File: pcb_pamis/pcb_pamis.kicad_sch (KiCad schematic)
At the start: 1 part, among them U1 ESP32-WROOM-32UE

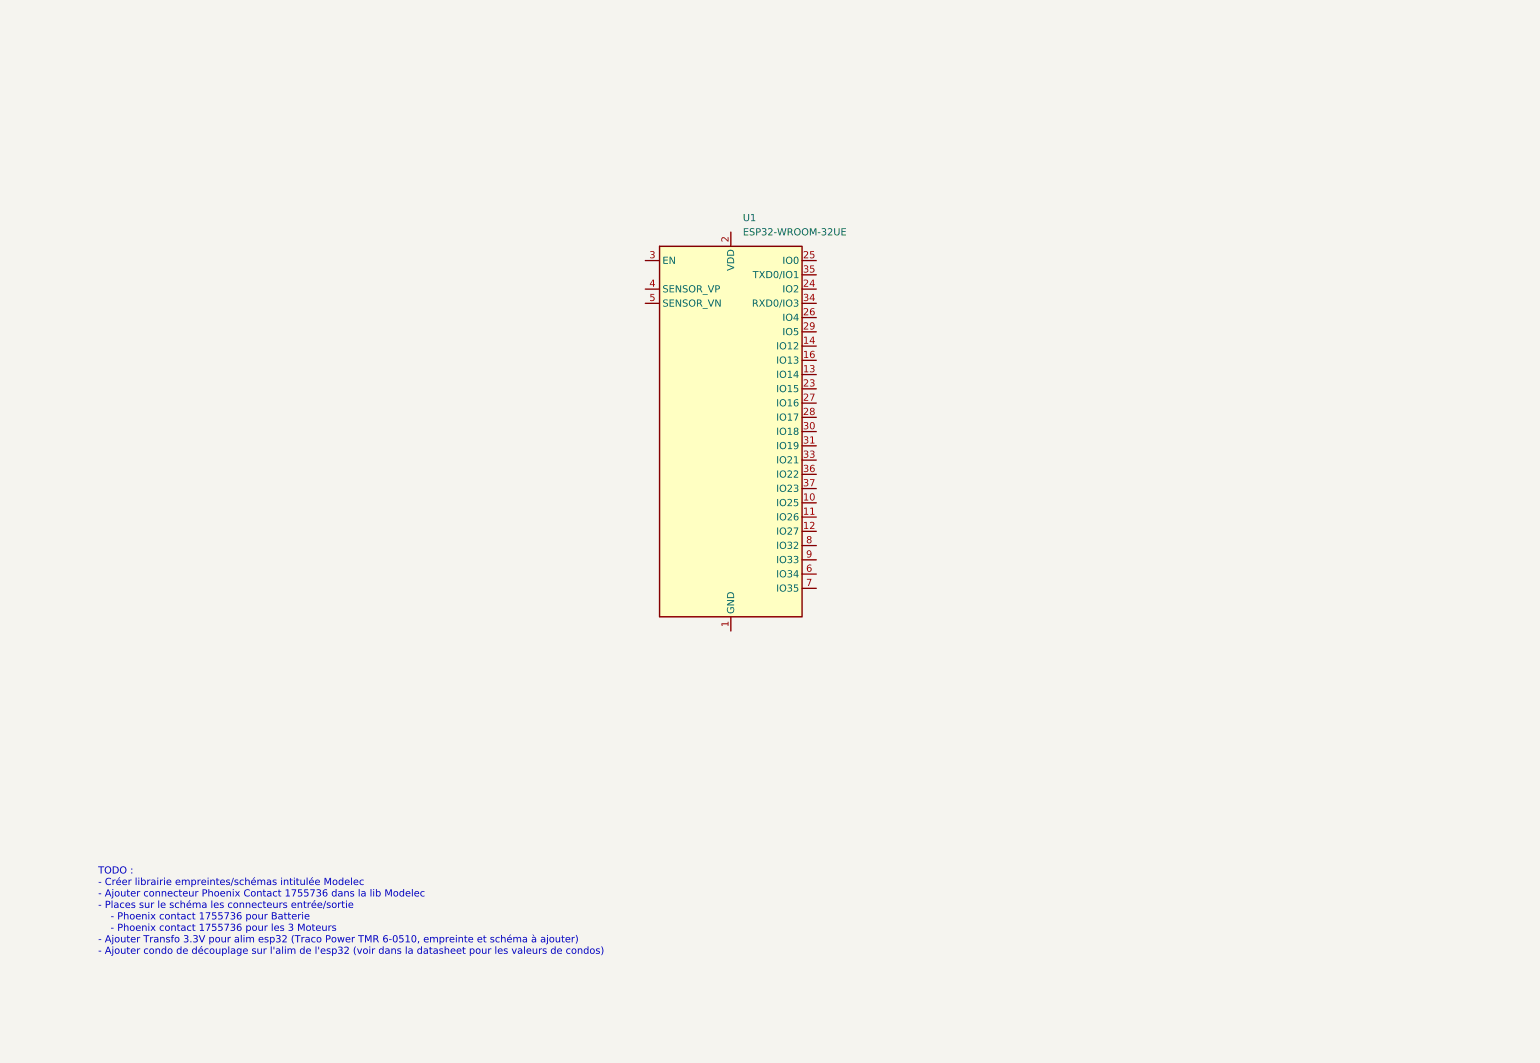
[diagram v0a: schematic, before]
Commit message: work on power supply
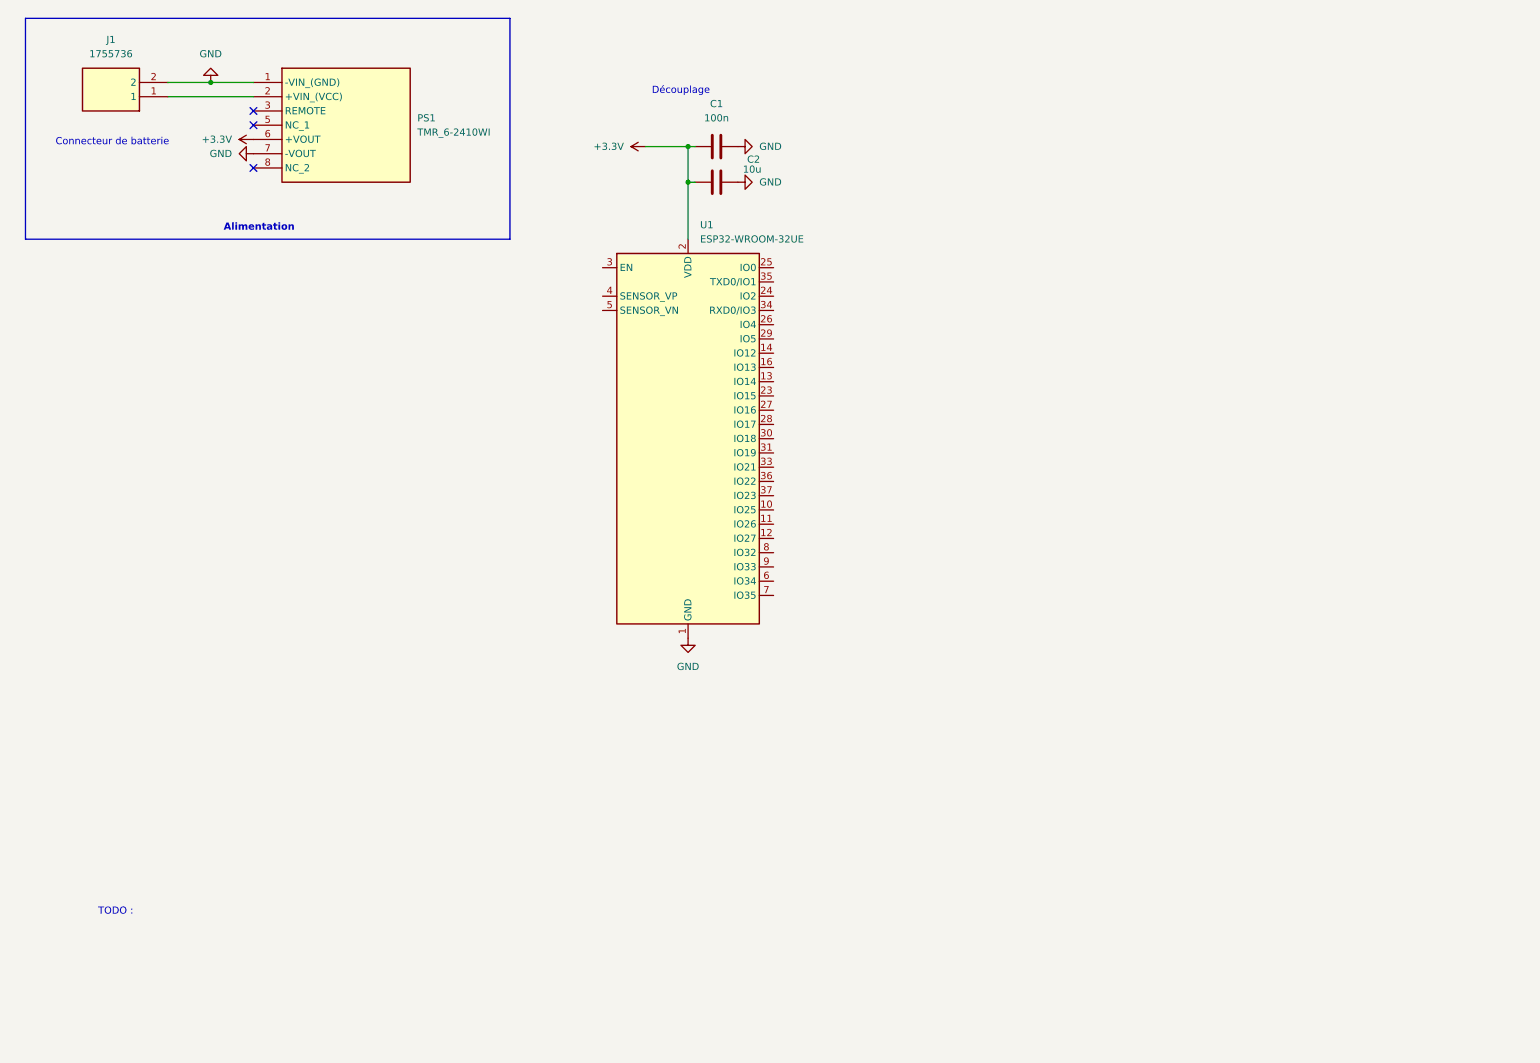
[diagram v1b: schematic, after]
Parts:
- added C1: 100n, Capacitor_SMD:C_0805_2012Metric_Pad1.18x1.45mm_HandSolder, symbol Device:C
- added C2: 10u, Capacitor_SMD:C_0805_2012Metric_Pad1.18x1.45mm_HandSolder, symbol Device:C
- added J1: 1755736, Modelec:PhoenixContact_MSTBVA_2,5_2-G-5,08_1x02_P5.08mm_Vertical, symbol Modelec:1755736
- added PS1: TMR_6-2410WI, TMR60510, symbol Modelec:TMR_6-0510
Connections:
- net GND: now reaches U1.1 (GND), U1.15 (GND), U1.38 (GND), U1.39 (GND)
- net GND: now also C1.2, C2.2, J1.2, PS1.1 (-VIN_(GND)), PS1.7 (-VOUT)
- net +3.3V: now reaches U1.2 (VDD)
- net +3.3V: now also C1.1, C2.1, PS1.6 (+VOUT)
- new net: J1.1, PS1.2 (+VIN_(VCC))
- no-connect marks 0 -> 3
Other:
- note added: "Alimentation"
- note added: "Connecteur de batterie"
- note added: "Découplage"
- note added: "TODO :"
- note removed: "TODO : - Créer librairie empreintes/schémas intitulée Modelec - Ajouter connecteur Phoenix Contact 1755736 dans la lib Modelec - Places sur le schéma les connecteurs entrée/sortie - Phoenix contact 1755736 pour Batterie - Phoenix contact 1755736 pour les 3 Moteurs - Ajouter Transfo 3.3V pour alim esp32 (Traco Power TMR 6-0510, empreinte et schéma à ajouter) - Ajouter condo de découplage sur l'ali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"
- moved on the sheet: U1

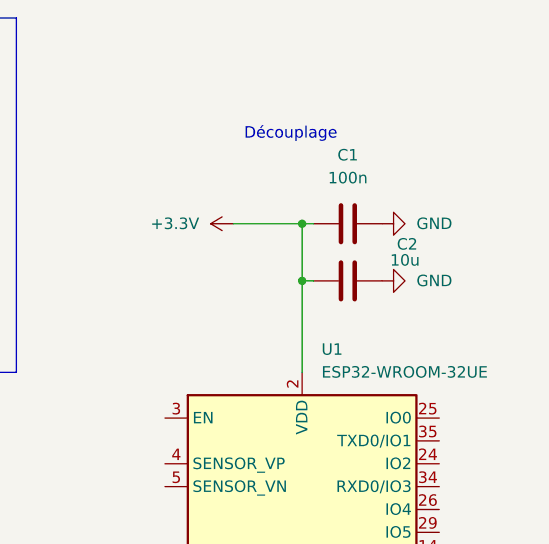
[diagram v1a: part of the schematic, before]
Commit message: fix: decouplage esp32
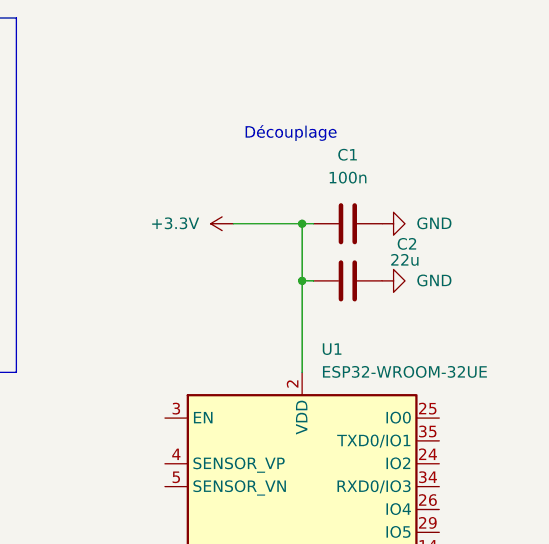
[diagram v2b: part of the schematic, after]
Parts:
- C2: value 10u -> 22u
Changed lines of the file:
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@@
 			)
 		)
-		(property "Value" "10u"
+		(property "Value" "22u"
 			(at 144.78 40.894 90)
 			(effects

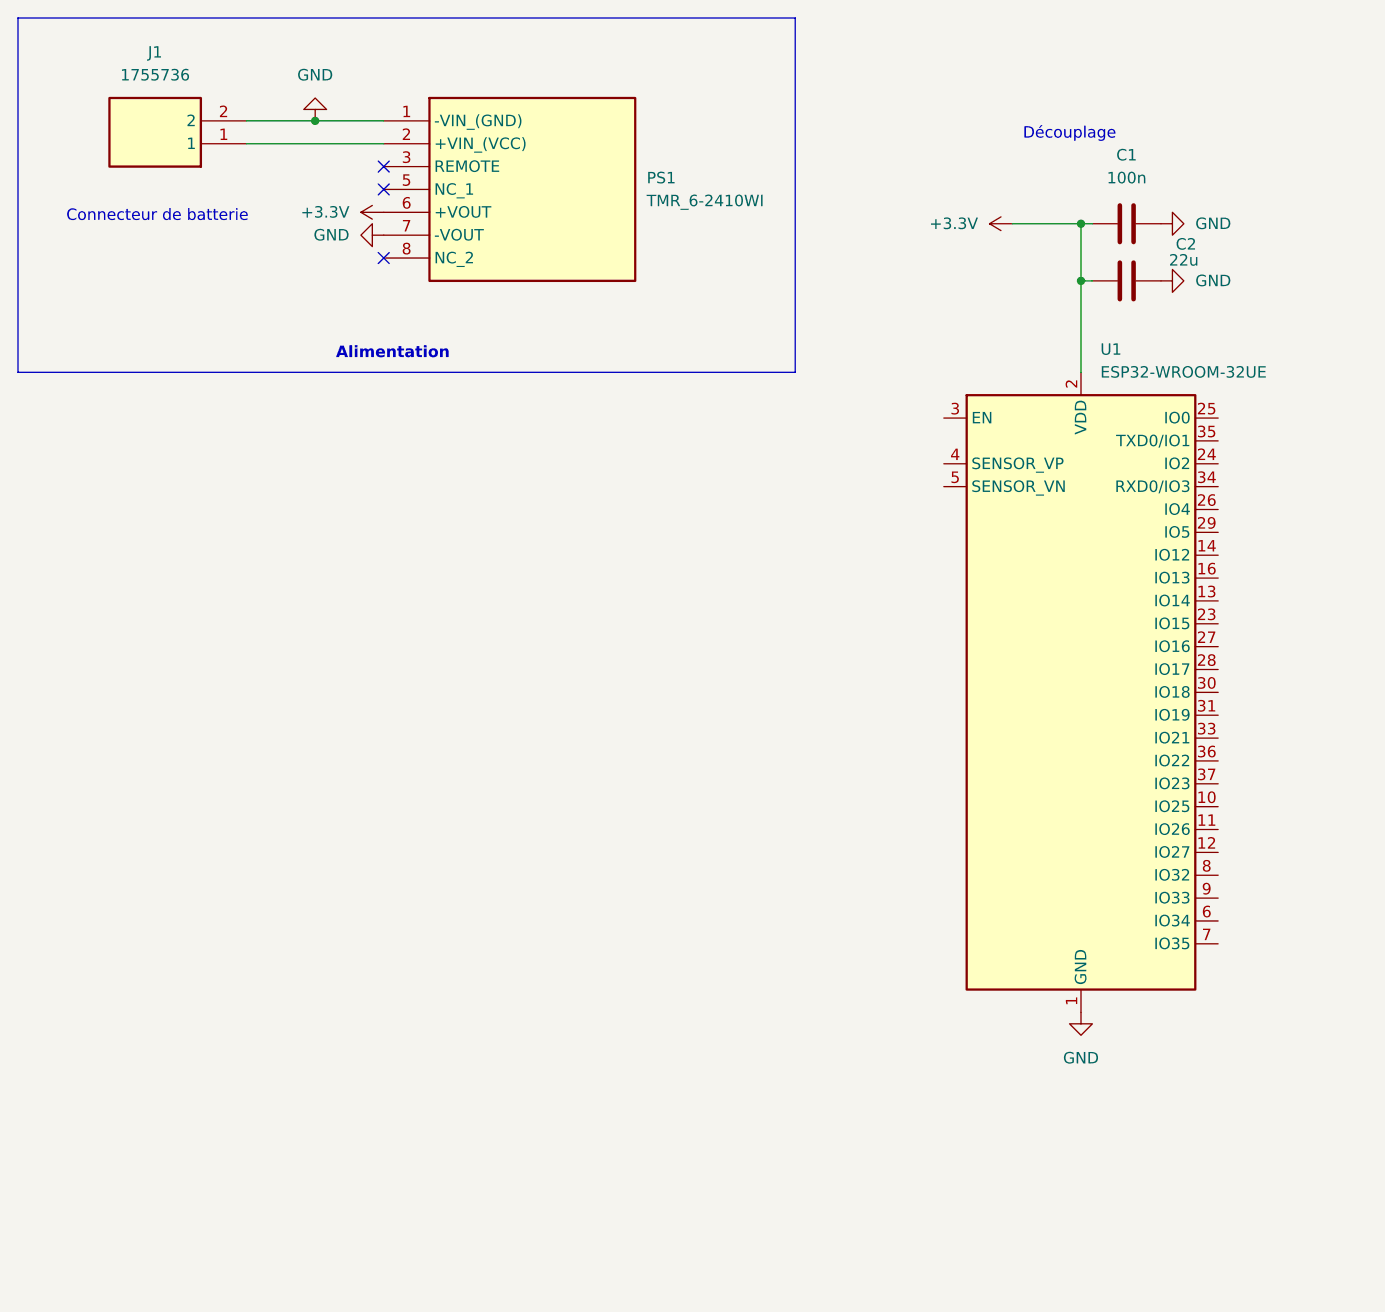
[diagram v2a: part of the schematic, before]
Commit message: feat: add usb port + add RESET button
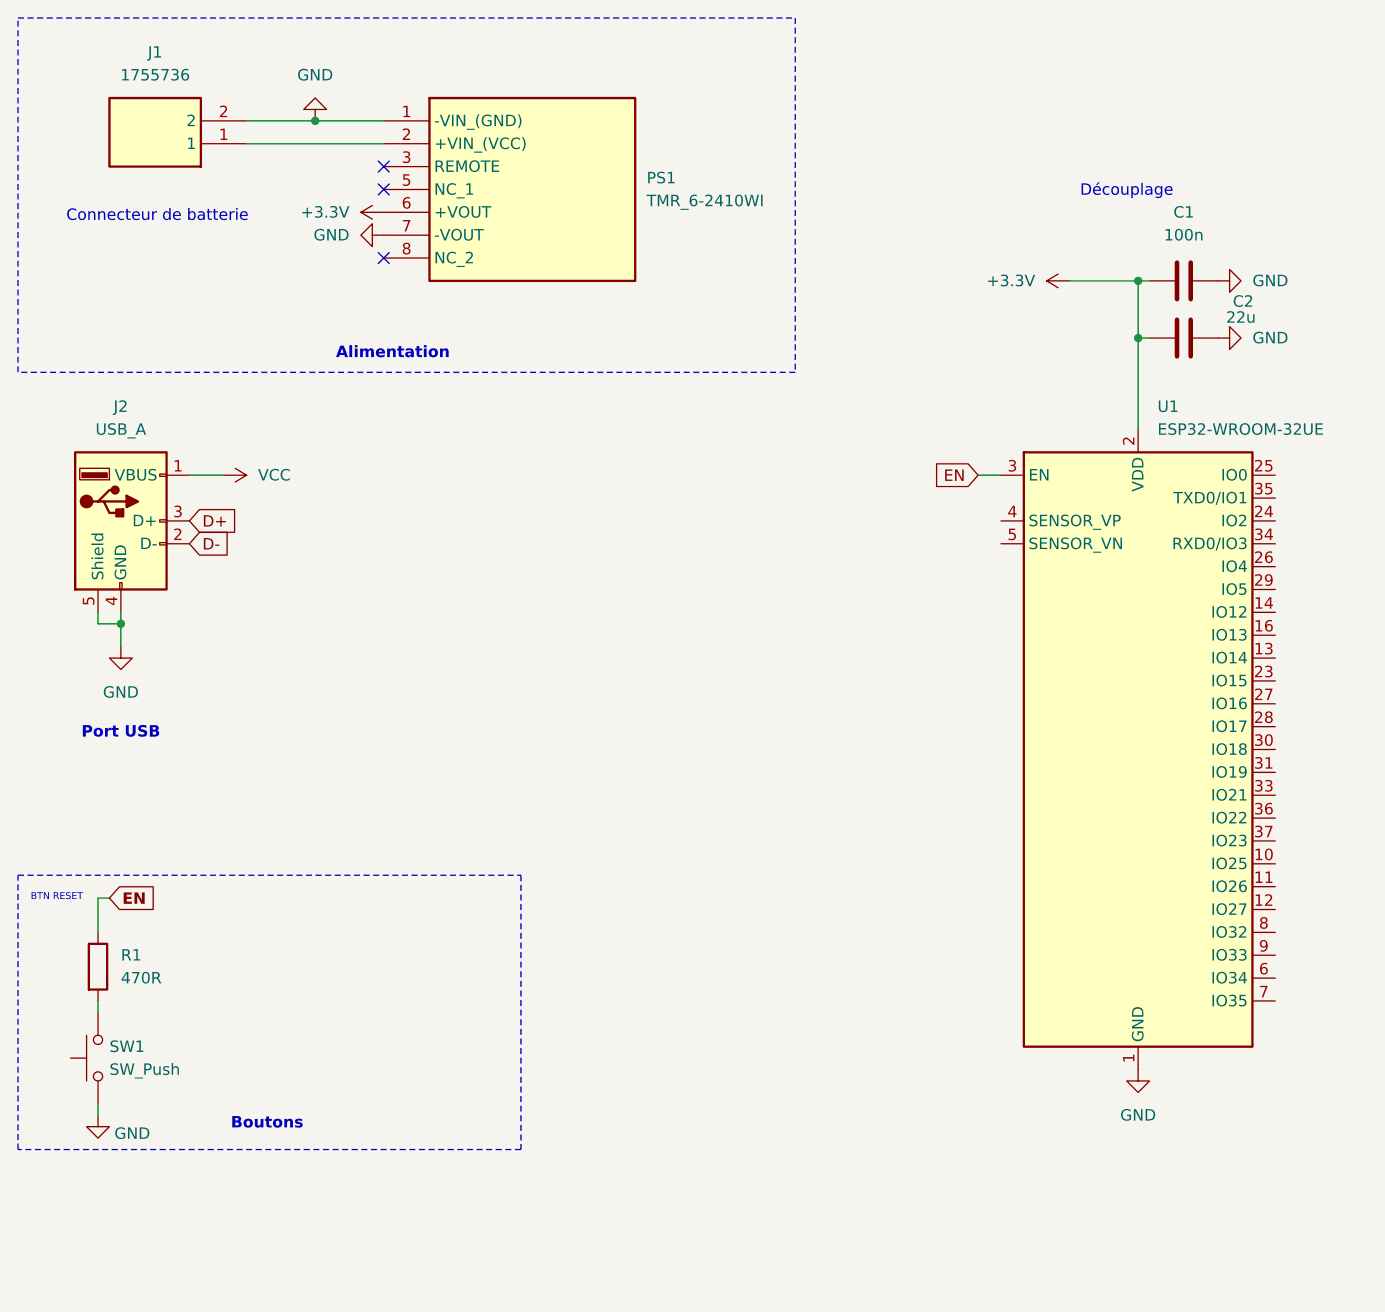
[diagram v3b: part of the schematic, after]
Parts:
- added J2: USB_A, Connector_USB:USB_A_Receptacle_GCT_USB1046, symbol Connector:USB_A
- added R1: 470R, symbol Device:R
- added SW1: SW_Push, symbol Switch:SW_Push
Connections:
- net GND: now also J2.4 (GND), J2.5 (Shield), SW1.1
- net EN: now reaches U1.3 (EN)
- net EN: now also R1.1
- new net: R1.2, SW1.2
- new net D+: J2.3 (D+)
- new net D-: J2.2 (D-)
- new net VCC: J2.1 (VBUS)
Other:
- note added: "BTN RESET"
- note added: "Boutons"
- note added: "Port USB"
- moved on the sheet: C1, C2, U1
